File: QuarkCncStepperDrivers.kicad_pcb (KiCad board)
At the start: 4 copper layers, 38.1 x 73.7 mm, 74 parts, among them J1 Conn_01x14, J2 Conn_01x14, Q1 AO4264E, Q2 AO4264E, Q3 AO4264E, Q4 AO4264E, Q5 AO4264E, Q6 AO4264E, Q7 AO4264E, Q8 AO4264E, SW1 SW_DIP_x04, SW2 SW_DIP_x04, U1 TMC2160A-TA-T

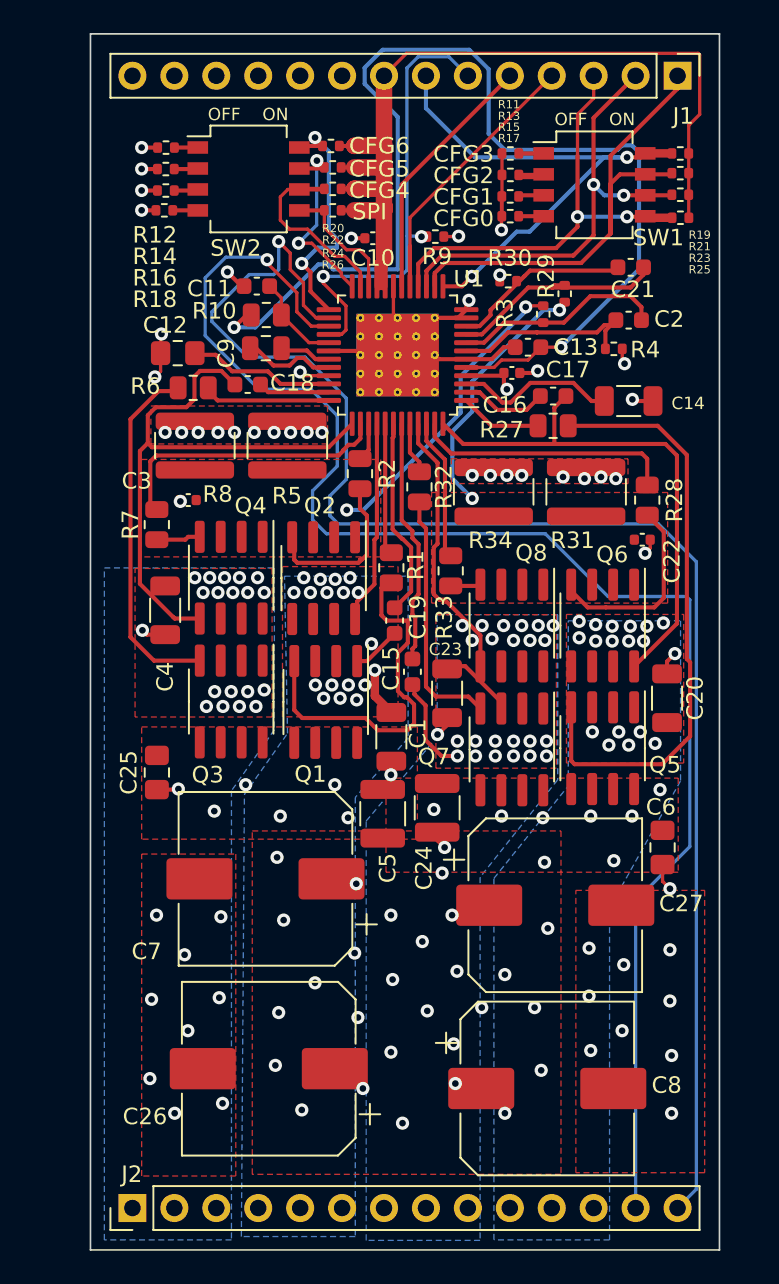
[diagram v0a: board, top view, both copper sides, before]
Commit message: Removed caps from board. Will be placed on main board
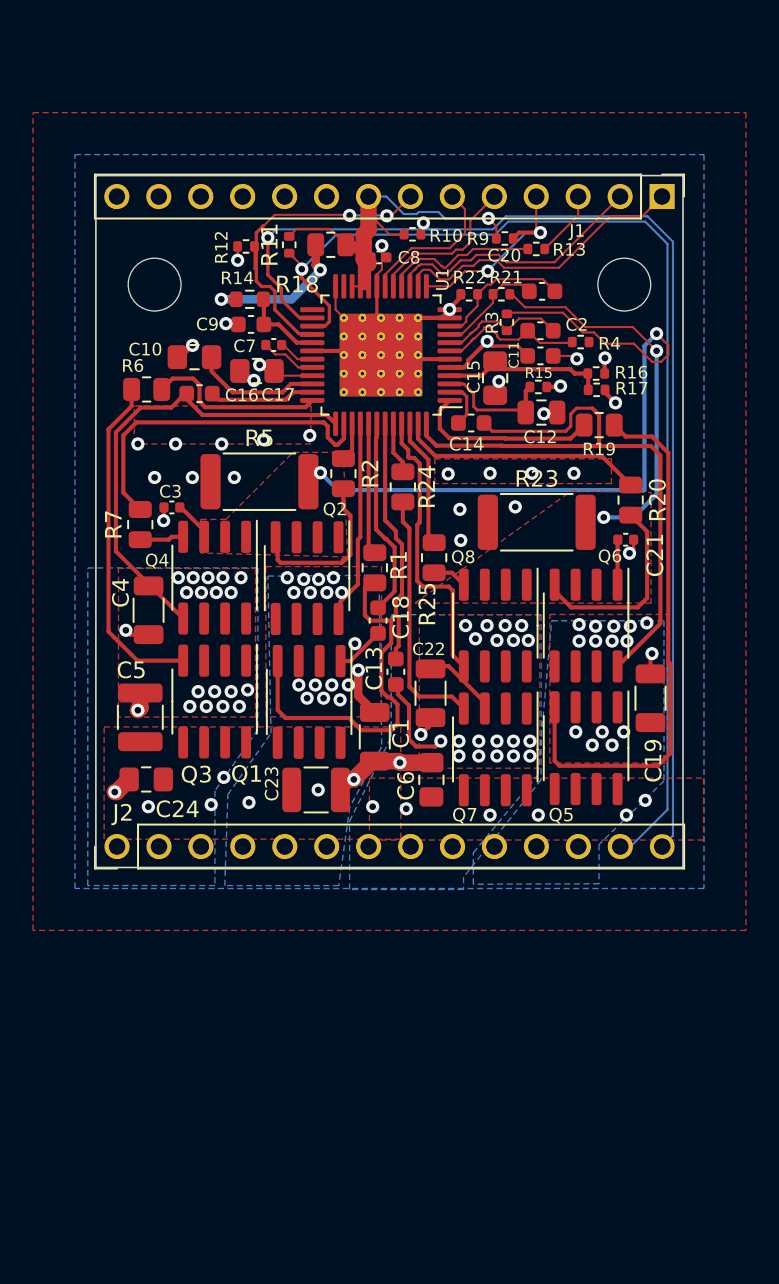
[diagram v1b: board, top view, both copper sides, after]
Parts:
- removed C26, C27: 100u 80V, Capacitor_SMD:CP_Elec_10x10
- removed the C7 at (110.6, 146.1)
- removed the C8 at (127.7, 158.8)
- removed the R12 at (104.6, 101.8)
- removed the R14 at (104.6, 103.1)
- removed the R19 at (135.7, 102.2)
- removed the R20 at (114.6, 101.7)
- removed the R21 at (135.7, 103.4)
- removed the R22 at (114.7, 103.0)
- removed the R23 at (135.7, 104.7)
- removed the R24 at (114.7, 104.3)
- removed the R25 at (135.7, 106.1)
- removed R26: 100k 1%, Resistor_SMD:R_0402_1005Metric
- removed R34, R8: 100mR 1W, Resistor_SMD:R_1218_3246Metric
- removed SW1, SW2: SW_DIP_x04, Button_Switch_SMD:SW_DIP_SPSTx04_Slide_Omron_A6H-4101_W6.15mm_P1.27mm
- added C15: 100n 100V, Capacitor_SMD:C_0805_2012Metric_Pad1.18x1.45mm_HandSolder, F.Cu at (124.5, 115.8)
- added H1: MountingHole, MountingHole:MountingHole_3.2mm_M3, F.Cu at (103.9, 110.1)
- added H2: MountingHole, MountingHole:MountingHole_3.2mm_M3, F.Cu at (132.3, 110.1)
- added R10: 10k 1%, Resistor_SMD:R_0402_1005Metric, F.Cu at (119.5, 107.1)
- added R9: 10k 1%, Resistor_SMD:R_0402_1005Metric, F.Cu at (125.1, 107.3)
- C12: renamed from C14; footprint Capacitor_SMD:C_1206_3216Metric -> Capacitor_SMD:C_0805_2012Metric
- C17: value 100n 50V -> 100n 100V; footprint Capacitor_SMD:C_0402_1005Metric -> Capacitor_SMD:C_0805_2012Metric_Pad1.18x1.45mm_HandSolder
- C7: renamed from C9; footprint Capacitor_SMD:C_0805_2012Metric -> Capacitor_SMD:C_0402_1005Metric
- R12: renamed from R9; value 100k 1% -> 10k 1%
- R13: value 10k 1% -> 33
- R14: renamed from R10; footprint Resistor_SMD:R_0805_2012Metric -> Resistor_SMD:R_0603_1608Metric
- R15: value 10k 1% -> 0R
- R16, R17: value 10k 1% -> 0R DNI
- R18: value 10k 1% -> 0R DNI; footprint Resistor_SMD:R_0402_1005Metric -> Resistor_SMD:R_0805_2012Metric
- R23: renamed from R31; value 100mR 1W -> 30mR 2W; footprint Resistor_SMD:R_1218_3246Metric -> Resistor_SMD:R_2512_6332Metric
- R5: value 100mR 1W -> 30mR 2W; footprint Resistor_SMD:R_1218_3246Metric -> Resistor_SMD:R_2512_6332Metric
- moved R16 28.3 mm to (130.6, 115.5)
- moved J2 21.9 mm to (101.6, 144.1)
- moved C5 15.8 mm to (103.0, 136.3)
- moved C17 15.4 mm to (110.1, 115.3), turned to 180 degrees
- moved C6 14.6 mm to (120.7, 140.1), turned to 90 degrees
- moved R11 14.5 mm to (112.0, 107.7), turned to 90 degrees
- moved R17 11.7 mm to (130.7, 116.5)
- moved R15 11.7 mm to (127.1, 116.3)
- moved R12 11.5 mm to (109.4, 107.8), turned to 0 degrees
- moved R18 10.3 mm to (114.6, 107.7), turned to 180 degrees
- moved C23 7.41 mm to (113.7, 140.7), turned to 0 degrees
- moved J1 7.38 mm to (134.6, 104.8)
- moved C20 5.56 mm to (127.4, 110.5), turned to 0 degrees
- moved C2 5.38 mm to (127.3, 112.9)
- moved C12 5.33 mm to (127.3, 117.9)
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- renumbered C12 to C10, C13 to C11, C15 to C13, C16 to C14, C18 to C16, C19 to C18, C20 to C19, C21 to C20, C22 to C21, C23 to C22, C24 to C23, C25 to C24, C10 to C8, C11 to C9, R27 to R19, R28 to R20, R29 to R21, R30 to R22, R32 to R24, R33 to R25
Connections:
- C11 pad 1: Net-(C13-Pad1) -> /STEPPER DRIVER X/5VOUT
- J1 pad 4: /STEPPER_X_STEP -> /STEPPER_X_CSn
- J1 pad 5: /STEPPER_X_DIR -> /STEPPER_X_STEP
- J1 pad 6: /STEPPER_X_ENn -> /STEPPER_X_DIR
- J1 pad 7: /STEPPER_X_CSn -> /STEPPER_X_ENn
- J1 pad 9: VCC -> +12V
- R11 pad 1: GND -> /STEPPER_DIAG1
- R11 pad 2: Net-(R11-Pad2) -> +3V3
- R13 pad 1: GND -> Net-(R13-Pad1)
- R13 pad 2: Net-(R13-Pad2) -> /STEPPER_MISO
- R14 pad 2: Net-(C13-Pad1) -> /STEPPER DRIVER X/5VOUT
- R15 pad 1: GND -> /STEPPER DRIVER X/TMC5160_12VOUT
- R15 pad 2: Net-(R15-Pad2) -> +12V
- R16 pad 1: GND -> /STEPPER DRIVER X/VSA
- R16 pad 2: Net-(R16-Pad2) -> +12V
- R17 pad 1: GND -> /STEPPER DRIVER X/VSA
- R17 pad 2: Net-(R17-Pad2) -> VCC
- R18 pad 1: GND -> +3V3
- R18 pad 2: Net-(R18-Pad2) -> /STEPPER DRIVER X/5VOUT
- U1 pad 16: /STEPPER_MISO -> Net-(R13-Pad1)
- U1 pad 22: /STEPPER DRIVER X/SPI_MODE -> +3V3
- U1 pad 23: /STEPPER DRIVER X/CFG4 -> unconnected-(U1-Pad23)
- U1 pad 24: /STEPPER DRIVER X/CFG5 -> GND
- U1 pad 25: /STEPPER DRIVER X/CFG6 -> unconnected-(U1-Pad25)
- U1 pad 4: VCC -> /STEPPER DRIVER X/VSA
- U1 pad 5: Net-(C13-Pad1) -> /STEPPER DRIVER X/5VOUT
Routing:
- net Net-(C13-Pad1): track 68.2 -> 0.00 mm, vias 2 -> 0
- net +3V3: track 54.9 -> 26.4 mm, vias 0 -> 1
- net /STEPPER DRIVER X/5VOUT: track 0.00 -> 27.5 mm, vias 0 -> 3
- net /STEPPER DRIVER X/hbridge_A3/hbridge_low_side: track 18.5 -> 45.0 mm
- net +12V: track 0.00 -> 25.8 mm, vias 0 -> 2
- net /STEPPER_DIAG1: track 94.0 -> 68.5 mm
- net /STEPPER_DIAG2: track 94.3 -> 70.9 mm, vias 1 -> 2
- net /STEPPER_MISO: track 27.3 -> 4.02 mm, vias 2 -> 0
- net /STEPPER_X_CSn: track 32.6 -> 12.4 mm
- net GND: track 52.5 -> 35.7 mm, vias 58 -> 32
- net /STEPPER DRIVER X/CFG6: track 15.4 -> 0.00 mm, vias 2 -> 0
- net /STEPPER_SCK: track 30.7 -> 18.3 mm
- net /STEPPER DRIVER X/CFG4: track 12.2 -> 0.00 mm
- net /STEPPER DRIVER X/CFG5: track 12.1 -> 0.00 mm, vias 2 -> 0
- net /STEPPER_MOSI: track 27.7 -> 16.3 mm, vias 2 -> 0
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- added copper zone on B.Cu, net GND
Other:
- board size 38.1 x 73.7 mm -> 35.6 x 41.9 mm
- board text removed: "3V3"
- board text removed: "A1"
- board text removed: "A2"
- board text removed: "B1"
- board text removed: "B2"
- board text removed: "CFG0"
- board text removed: "CFG1"
- board text removed: "CFG2"
- board text removed: "CFG3"
- board text removed: "CFG4"
- board text removed: "CFG5"
- board text removed: "CFG6"
- board text removed: "CSn"
- board text removed: "DIAG1"
- board text removed: "DIAG2"
- board text removed: "DIR"
- board text removed: "ENn"
- board text removed: "GND"
- board text removed: "MISO"
- board text removed: "MOSI"
- board text removed: "OFF"
- board text removed: "ON"
- board text removed: "SCK"
- board text removed: "SPI"
- board text removed: "STEP"
- board text removed: "VCC"
